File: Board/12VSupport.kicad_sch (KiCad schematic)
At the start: 40 parts, among them J1 12V, J2 BATT, J3 BUCK_IN, J4 BUCK_OUT, J5 BOOST_IN, J6 BOOST_OUT, J8 HEATER, K1 SLA-05VDC-SL-C, K2 SLA-05VDC-SL-C, K3 SLA-05VDC-SL-C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

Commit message: Minor improvements
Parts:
- added C10: 100n, Capacitor_SMD:C_0805_2012Metric, symbol Device:C
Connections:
- net B-: now reaches F1.2, K1.11A, K1.11B
- net B-: now also C10.2
- net B+: now reaches K2.11A, K2.11B, U4.3 (IP-), U4.4 (IP-)
- net B+: now also C10.1
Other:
- moved on the sheet: F1
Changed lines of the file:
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@@
 	)
 	(junction
+		(at 59.69 134.62)
+		(diameter 0)
+		(color 0 0 0 0)
+	)
+	(junction
 		(at 49.53 73.66)
 		(diameter 0)
@@
 	)
 	(junction
+		(at 59.69 114.3)
+		(diameter 0)
+		(color 0 0 0 0)
+	)
+	(junction
 		(at 203.2 66.04)
 		(diameter 0)
@@
 	)
 	(junction
+		(at 54.61 134.62)
+		(diameter 0)
+		(color 0 0 0 0)
+	)
+	(junction
 		(at 46.99 33.02)
 		(diameter 0)
@@
 	)
 	(junction
+		(at 59.69 118.11)
+		(diameter 0)
+		(color 0 0 0 0)
+	)
+	(junction
 		(at 105.41 163.83)
 		(diameter 0)
@@
 	(wire
 		(pts
+			(xy 63.5 118.11) (xy 59.69 118.11)
+		)
+		(stroke
+			(width 0)
+			(type default)
+		)
+	)
+	(wire
+		(pts
 			(xy 33.02 52.07) (xy 46.99 52.07)
 		)
@@
 	(wire
 		(pts
+			(xy 54.61 116.84) (xy 43.18 116.84)
+		)
+		(stroke
+			(width 0)
+			(type default)
+		)
+	)
+	(wire
+		(pts
 			(xy 82.55 153.67) (xy 80.01 153.67)
 		)
@@
 	(wire
 		(pts
+			(xy 54.61 116.84) (xy 54.61 134.62)
+		)
+		(stroke
+			(width 0)
+			(type default)
+		)
+	)
+	(wire
+		(pts
 			(xy 53.34 38.1) (xy 53.34 52.07)
 		)
@@
 	(wire
 		(pts
+			(xy 59.69 129.54) (xy 59.69 134.62)
+		)
+		(stroke
+			(width 0)
+			(type default)
+		)
+	)
+	(wire
+		(pts
 			(xy 46.99 52.07) (xy 53.34 52.07)
 		)
@@
 	(wire
 		(pts
+			(xy 59.69 114.3) (xy 82.55 114.3)
+		)
+		(stroke
+			(width 0)
+			(type default)
+		)
+	)
+	(wire
+		(pts
 			(xy 45.72 144.78) (xy 45.72 143.51)
 		)
@@
 	(wire
 		(pts
-			(xy 105.41 163.83) (xy 105.41 171.45)
+			(xy 54.61 134.62) (xy 54.61 143.51)
 		)
 		(stroke
@@
 	(wire
 		(pts
-			(xy 36.83 114.3) (xy 82.55 114.3)
+			(xy 105.41 163.83) (xy 105.41 171.45)
 		)
 		(stroke
@@
 	(wire
 		(pts
-			(xy 110.49 146.05) (xy 115.57 146.05)
+			(xy 36.83 114.3) (xy 59.69 114.3)
 		)
 		(stroke
@@
 	(wire
 		(pts
-			(xy 46.99 48.26) (xy 46.99 52.07)
+			(xy 110.49 146.05) (xy 115.57 146.05)
 		)
 		(stroke
@@
 	(wire
 		(pts
-			(xy 250.19 57.15) (xy 250.19 52.07)
+			(xy 46.99 48.26) (xy 46.99 52.07)
 		)
 		(stroke
@@
 	(wire
 		(pts
-			(xy 48.26 116.84) (xy 77.47 116.84)
+			(xy 250.19 57.15) (xy 250.19 52.07)
 		)
 		(stroke
@@
 	(wire
 		(pts
+			(xy 59.69 118.11) (xy 59.69 114.3)
+		)
+		(stroke
+			(width 0)
+			(type default)
+		)
+	)
+	(wire
+		(pts
 			(xy 80.01 124.46) (xy 82.55 124.46)
 		)
@@
 	(wire
 		(pts
+			(xy 59.69 118.11) (xy 59.69 121.92)
+		)
+		(stroke
+			(width 0)
+			(type default)
+		)
+	)
+	(wire
+		(pts
 			(xy 171.45 109.22) (xy 171.45 140.97)
 		)
@@
 	(wire
 		(pts
-			(xy 24.13 116.84) (xy 40.64 116.84)
+			(xy 24.13 116.84) (xy 35.56 116.84)
 		)
 		(stroke
@@
 	(wire
 		(pts
+			(xy 54.61 143.51) (xy 82.55 143.51)
+		)
+		(stroke
+			(width 0)
+			(type default)
+		)
+	)
+	(wire
+		(pts
 			(xy 110.49 143.51) (xy 115.57 143.51)
 		)
@@
 	(wire
 		(pts
-			(xy 163.83 66.04) (xy 163.83 88.9)
+			(xy 54.61 134.62) (xy 59.69 134.62)
 		)
 		(stroke
@@
 	(wire
 		(pts
-			(xy 26.67 147.32) (xy 26.67 156.21)
+			(xy 163.83 66.04) (xy 163.83 88.9)
 		)
 		(stroke
@@
 	(wire
 		(pts
-			(xy 45.72 156.21) (xy 45.72 154.94)
+			(xy 26.67 147.32) (xy 26.67 156.21)
 		)
 		(stroke
@@
 	(wire
 		(pts
-			(xy 180.34 109.22) (xy 171.45 109.22)
+			(xy 45.72 156.21) (xy 45.72 154.94)
 		)
 		(stroke
@@
 	(wire
 		(pts
-			(xy 179.07 66.04) (xy 163.83 66.04)
+			(xy 180.34 109.22) (xy 171.45 109.22)
 		)
 		(stroke
@@
 	(wire
 		(pts
-			(xy 203.2 86.36) (xy 203.2 133.35)
+			(xy 179.07 66.04) (xy 163.83 66.04)
 		)
 		(stroke
@@
 	(wire
 		(pts
-			(xy 82.55 143.51) (xy 77.47 143.51)
+			(xy 203.2 86.36) (xy 203.2 133.35)
 		)
 		(stroke
@@
 	(wire
 		(pts
-			(xy 49.53 71.12) (xy 49.53 73.66)
+			(xy 59.69 134.62) (xy 63.5 134.62)
 		)
 		(stroke
@@
 	(wire
 		(pts
-			(xy 149.86 91.44) (xy 163.83 91.44)
+			(xy 49.53 71.12) (xy 49.53 73.66)
 		)
 		(stroke
@@
 	(wire
 		(pts
-			(xy 77.47 116.84) (xy 77.47 143.51)
+			(xy 149.86 91.44) (xy 163.83 91.44)
 		)
 		(stroke
@@
 		)
 	)
+	(global_label "B+"
+		(shape output)
+		(at 63.5 118.11 0)
+		(fields_autoplaced yes)
+		(effects
+			(font
+				(size 1.27 1.27)
+			)
+			(justify left)
+		)
+		(property "Intersheetrefs" "${INTERSHEET_REFS}"
+			(at 69.3276 118.11 0)
+			(effects
+				(font
+					(size 1.27 1.27)
+				)
+				(justify left)
+				(hide yes)
+			)
+		)
+	)
 	(global_label "REL_HEATER"
 		(shape input)
@@
 		)
 	)
+	(global_label "B-"
+		(shape output)
+		(at 63.5 134.62 0)
+		(fields_autoplaced yes)
+		(effects
+			(font
+				(size 1.27 1.27)
+			)
+			(justify left)
+		)
+		(property "Intersheetrefs" "${INTERSHEET_REFS}"
+			(at 69.3276 134.62 0)
+			(effects
+				(font
+					(size 1.27 1.27)
+				)
+				(justify left)
+				(hide yes)
+			)
+		)
+	)
 	(global_label "REL_CHARGE"
 		(shape input)
@@
 	(symbol
 		(lib_id "Device:Fuse")
-		(at 44.45 116.84 90)
+		(at 39.37 116.84 90)
 		(mirror x)
 		(unit 1)
@@
 		(dnp no)
 		(property "Reference" "F1"
-			(at 44.45 123.19 90)
+			(at 39.37 123.19 90)
 			(effects
 				(font
@@
 		)
 		(property "Value" "20A"
-			(at 44.45 120.65 90)
+			(at 39.37 120.65 90)
 			(effects
 				(font
@@
 		)
 		(property "Footprint" "spetry:Fuseholder_Blade"
-			(at 44.45 115.062 90)
+			(at 39.37 115.062 90)
 			(effects
 				(font
@@
 		)
 		(property "Datasheet" "~"
-			(at 44.45 116.84 0)
+			(at 39.37 116.84 0)
 			(effects
 				(font
@@
 		)
 		(property "Description" "Fuse"
-			(at 44.45 116.84 0)
+			(at 39.37 116.84 0)
 			(effects
 				(font
@@
 					(unit 1)
 				)
+			)
+		)
+	)
+	(symbol
+		(lib_id "Device:C")
+		(at 59.69 125.73 0)
+		(unit 1)
+		(exclude_from_sim no)
+		(in_bom yes)
+		(on_board yes)
+		(dnp no)
+		(property "Reference" "C10"
+			(at 63.5 124.4599 0)
+			(effects
+				(font
+					(size 1.27 1.27)
+				)
+				(justify left)
+			)
+		)
+		(property "Value" "100n"
+			(at 63.5 126.9999 0)
+			(effects
+				(font
+					(size 1.27 1.27)
+				)
+				(justify left)
+			)
+		)
+		(property "Footprint" "Capacitor_SMD:C_0805_2012Metric"
+			(at 60.6552 129.54 0)
+			(effects
+				(font
+					(size 1.27 1.27)
+				)
+				(hide yes)
+			)
+		)
+		(property "Datasheet" "~"
+			(at 59.69 125.73 0)
+			(effects
+				(font
+					(size 1.27 1.27)
+				)
+				(hide yes)
+			)
+		)
+		(property "Description" "Unpolarized capacitor"
+			(at 59.69 125.73 0)
+			(effects
+				(font
+					(size 1.27 1.27)
+				)
+				(hide yes)
+			)
+		)
+		(pin "2"
+		)
+		(pin "1"
+		)
+		(instances
+			(project "12VSupport"
+				(path "/f0c44745-560b-4dea-806a-2541c74a511b"
+					(reference "C10")
+					(unit 1)
+				)

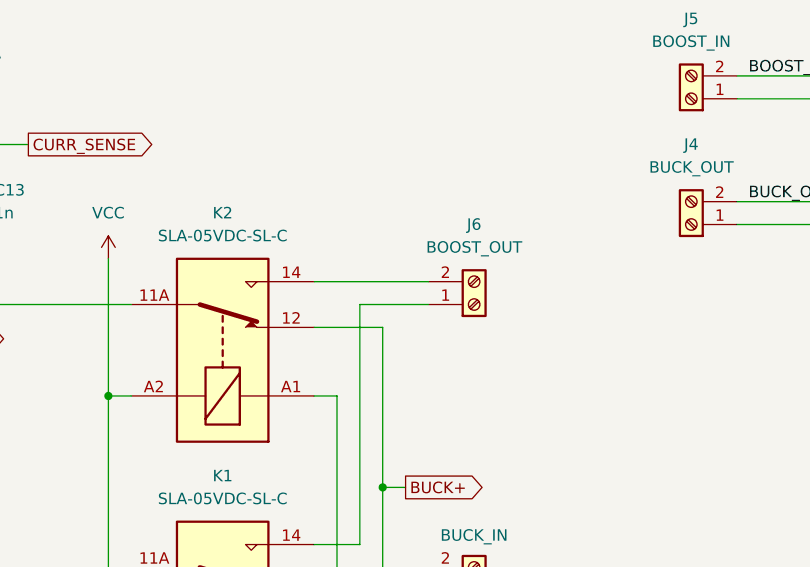
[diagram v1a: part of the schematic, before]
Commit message: Silkscreen fix
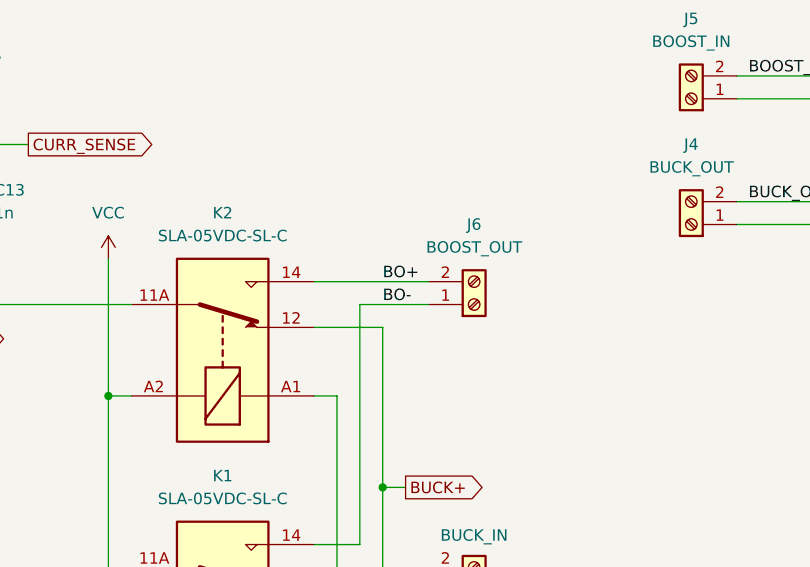
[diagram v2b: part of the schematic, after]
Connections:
- net BO-: now reaches J6.1 (Pin_1), K1.14
- net BO+: now reaches J6.2 (Pin_2), K2.14
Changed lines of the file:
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@@
+		)
+	)
+	(label "BO-"
+		(at 110.49 114.3 0)
+		(fields_autoplaced yes)
+		(effects
+			(font
+				(size 1.27 1.27)
+			)
+			(justify left bottom)
+		)
+	)
+	(label "BO+"
+		(at 110.49 111.76 0)
+		(fields_autoplaced yes)
+		(effects
+			(font
+				(size 1.27 1.27)
+			)
+			(justify left bottom)
 		)
 	)

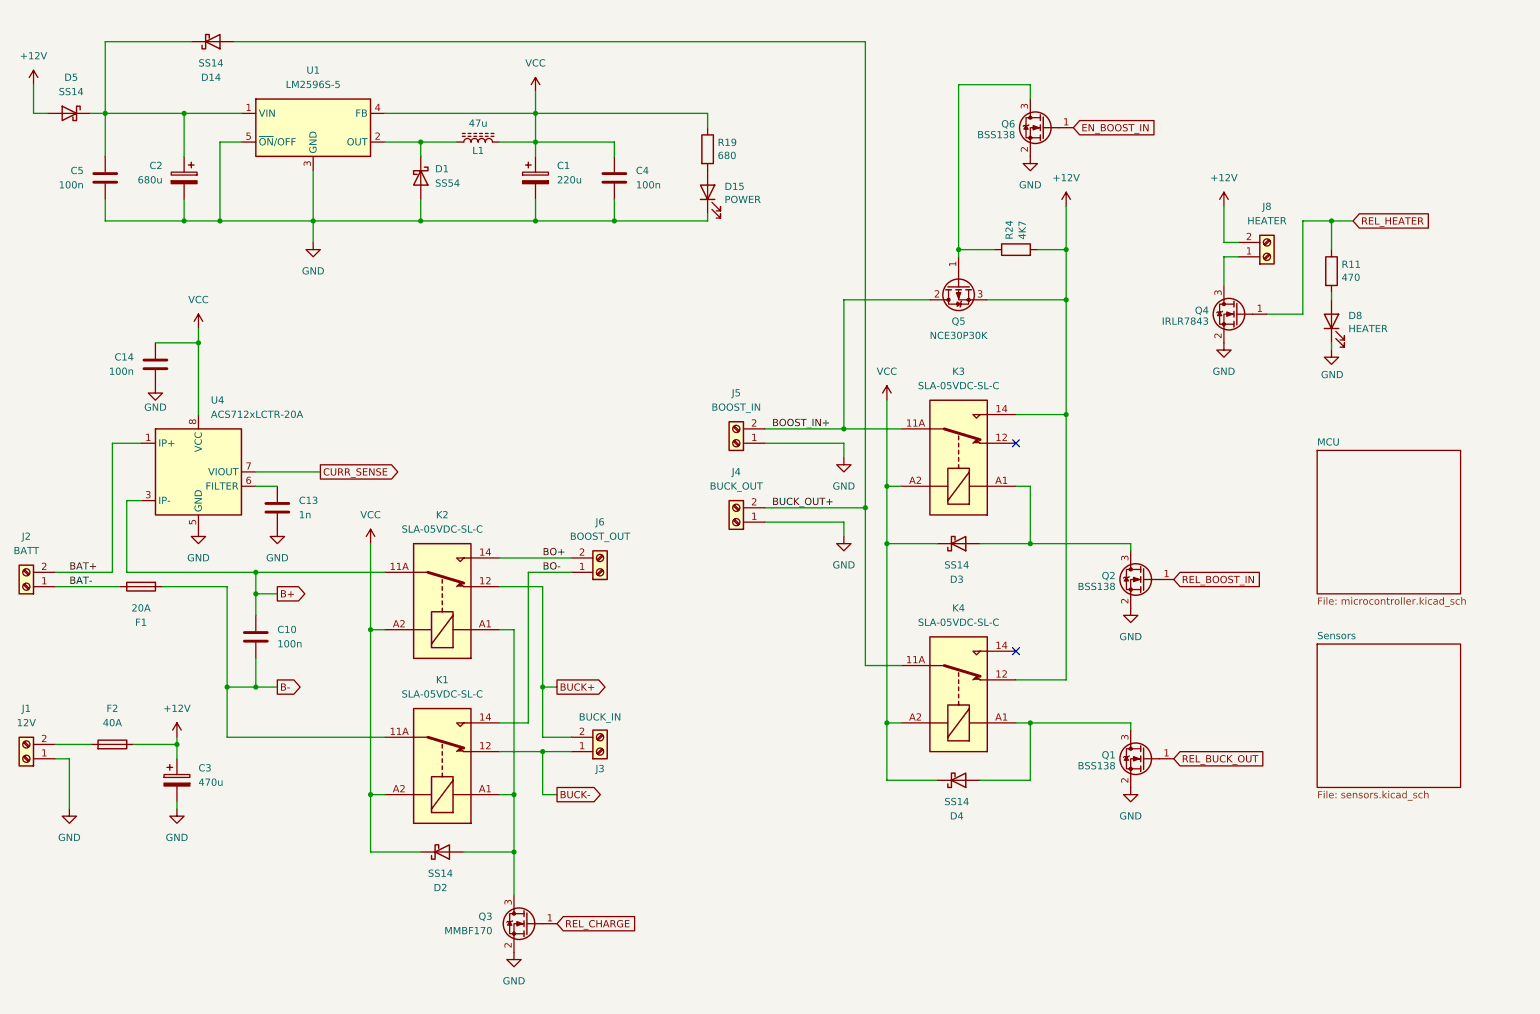
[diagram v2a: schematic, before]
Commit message: Set version number to 1.2. Various fixes. Add fan connector.
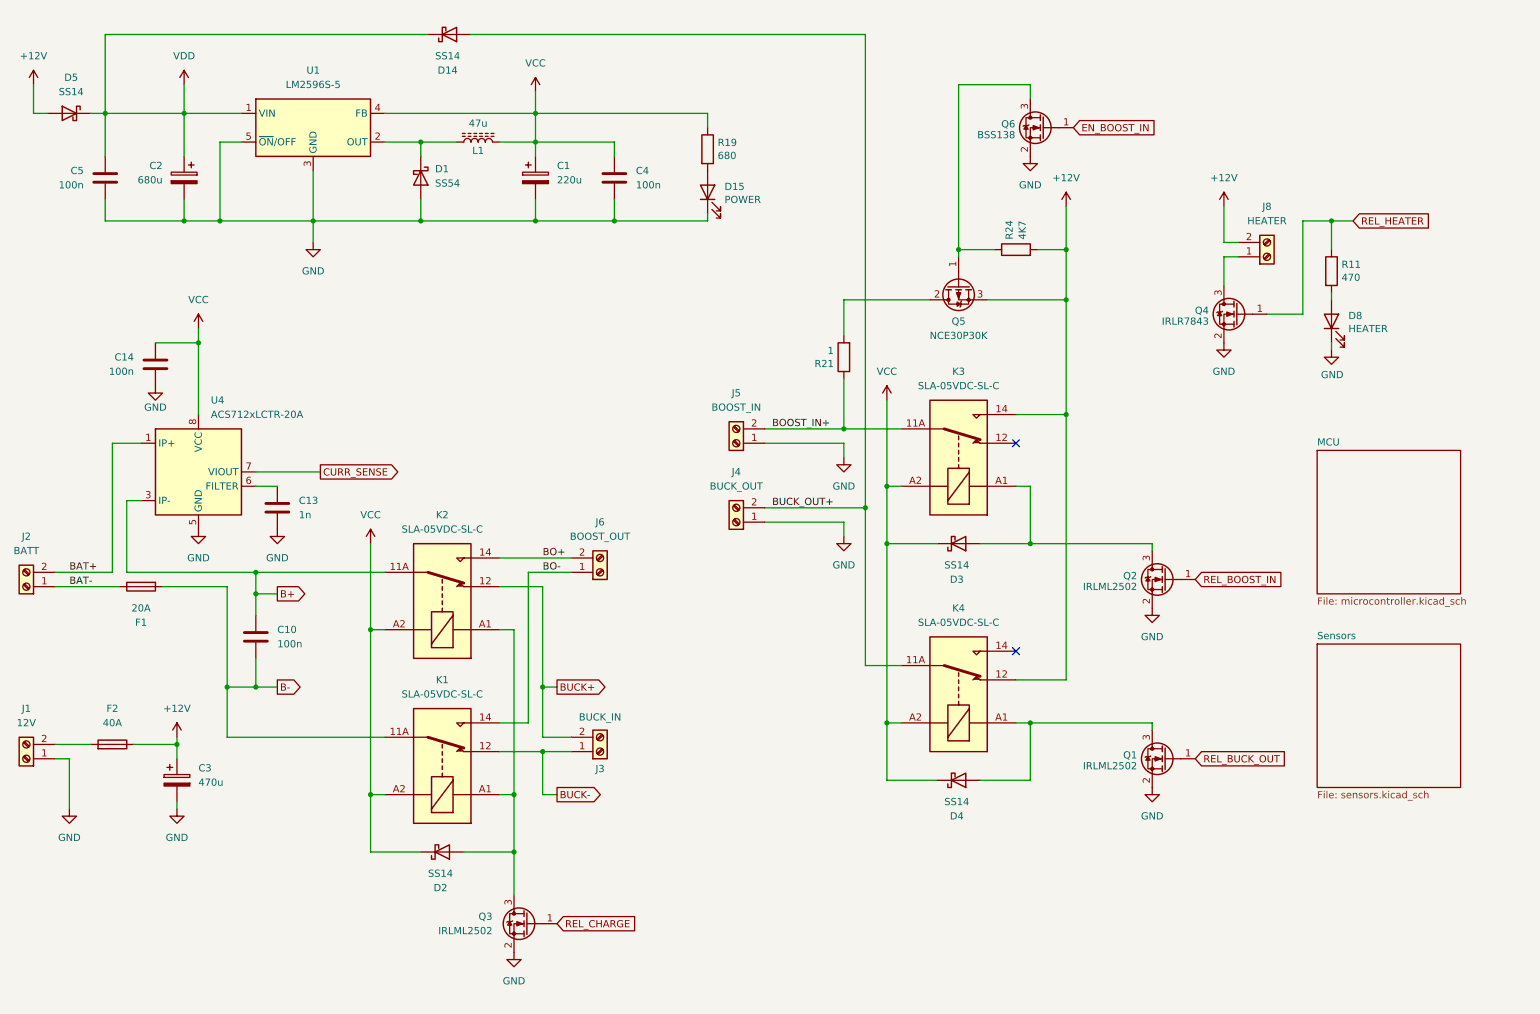
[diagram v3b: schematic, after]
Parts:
- added R21: 1, Resistor_SMD:R_2512_6332Metric, symbol Device:R
- Q1, Q2: value BSS138 -> IRLML2502
- Q3: value MMBF170 -> IRLML2502
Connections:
- net BOOST_IN+: now also R21.1; no longer Q5.2 (D)
- net VDD: now reaches C2.1, C5.1, D14.1 (K), D5.1 (K), U1.1 (VIN)
- new net: Q5.2 (D), R21.2
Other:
- moved on the sheet: D14, Q1, Q2

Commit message: Bugfixes
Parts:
- removed Q4: IRLR7843, Package_TO_SOT_SMD:TO-252-2, symbol Transistor_FET:BSS138
- added Q4: IRLR7843, Package_TO_SOT_SMD:TO-252-2, symbol Transistor_FET:STD7NK40Z
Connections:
- net BAT+: now also C10.1
- net BAT-: now also C10.2
- net GND: now also Q4.3 (S)
- net REL_HEATER: now also Q4.1 (G)
- net SYS_VOLTAGE: now reaches F2.2, J1.2 (Pin_2)
- net at J8.1 (Pin_1): now also Q4.2 (D)
- net B+: no longer names the net of K2.11A, K2.11B, U4.3 (IP-), U4.4 (IP-)
- net B+: no longer C10.1
- net B-: no longer names the net of F1.2, K1.11A, K1.11B
- net B-: no longer C10.2
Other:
- moved on the sheet: C10, C13, C14, D2, F1, J3, J6, K1, K2, Q3, U4

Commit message: Bugfixes
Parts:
- added C19, C20: 1000u, Capacitor_THT:CP_Radial_D13.0mm_P5.00mm, symbol Device:C_Polarized
- added C21, C22: 470u, Capacitor_THT:CP_Radial_D10.0mm_P5.00mm, symbol Device:C_Polarized
- added L4: 33u, Inductor_SMD:L_10.4x10.4_H4.8, symbol Device:L_Ferrite
- C1: footprint Capacitor_SMD:CP_Elec_6.3x7.7 -> Capacitor_THT:CP_Radial_D6.3mm_P2.50mm
- C2: footprint Capacitor_SMD:CP_Elec_10x10.5 -> Capacitor_THT:CP_Radial_D10.0mm_P5.00mm
- C3: value 470u -> 1000u; footprint Capacitor_SMD:CP_Elec_8x10.5 -> Capacitor_THT:CP_Radial_D13.0mm_P5.00mm
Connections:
- net +12V: now also C19.1, C21.1, C22.1
- net BAT+: now also C20.1
- net BAT-: now also C20.2
- net GND: now also C19.2, C21.2, C22.2
- net VCC: no longer C14.1, U4.8 (VCC)
- net VDD: now also L4.1; no longer D14.1 (K), D5.1 (K)
- new net: D14.1 (K), D5.1 (K), L4.2
- new net VCC_MCU: C14.1, U4.8 (VCC)
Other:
- moved on the sheet: C1, C2, C3, C4, C5, D1, D15, F2, J1, L1, R19, U1

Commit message: New layout
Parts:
- removed C19: 1000u, Capacitor_THT:CP_Radial_D13.0mm_P5.00mm, symbol Device:C_Polarized
- removed Q5: NCE30P30K, Package_TO_SOT_SMD:TO-252-2, symbol Transistor_FET:QM6015D
- removed Q6: BSS138, Package_TO_SOT_SMD:SOT-23, symbol Transistor_FET:BSS138
- removed R21: 1, Resistor_SMD:R_2512_6332Metric, symbol Device:R
- removed R24: 4K7, Resistor_SMD:R_0805_2012Metric, symbol Device:R
- C22: value 470u -> 220u; footprint Capacitor_THT:CP_Radial_D10.0mm_P5.00mm -> Capacitor_THT:CP_Radial_D6.3mm_P2.50mm
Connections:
- net +12V: no longer C22.1
- net BAT-: no longer C20.2
- net VCC: now also C22.1
- net at F1.2, K1.11A, K1.11B: now also C20.2
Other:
- moved on the sheet: C4, D15, R19
